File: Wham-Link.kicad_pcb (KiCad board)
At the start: 4 copper layers, 70 x 30 mm, 45 parts, among them J2 Conn_02x05_Counter_Clockwise, J3 Conn_01x09_Pin, SW2 SKRPACE010, SW3 SKRPACE010, U1 LAN8720A-CP-TR, U2 AMS1117-3.3, U3 CH340C, U4 ESP32-WROOM-32UE, X1 ECS-2520MV-250-CN-TR

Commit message: v0.1 Wham-Link for Layout Review
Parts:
- moved J2 0.30 mm to (175.8, 102.7)
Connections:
- J2 pad 1: GPI36 -> unconnected-(J2-Pin_1-Pad1)
- J2 pad 10: GP33 -> unconnected-(J2-Pin_10-Pad10)
- J2 pad 2: GPI39 -> unconnected-(J2-Pin_2-Pad2)
- J2 pad 3: GPI34 -> unconnected-(J2-Pin_3-Pad3)
- J2 pad 4: GPI35 -> unconnected-(J2-Pin_4-Pad4)
- J2 pad 6: GP14 -> unconnected-(J2-Pin_6-Pad6)
- J2 pad 7: GP16 -> GND
- J2 pad 8: GP17 -> unconnected-(J2-Pin_8-Pad8)
- J2 pad 9: GP32 -> unconnected-(J2-Pin_9-Pad9)
- J3 pad 2: unconnected-(J3-Pin_2-Pad2) -> +3V3
- J3 pad 3: unconnected-(J3-Pin_3-Pad3) -> GND
- J3 pad 4: unconnected-(J3-Pin_4-Pad4) -> GP14
- J3 pad 5: unconnected-(J3-Pin_5-Pad5) -> GP16
- J3 pad 6: unconnected-(J3-Pin_6-Pad6) -> GP13
- J3 pad 7: unconnected-(J3-Pin_7-Pad7) -> GP33
- J3 pad 8: unconnected-(J3-Pin_8-Pad8) -> GP32
- J3 pad 9: unconnected-(J3-Pin_9-Pad9) -> GP17
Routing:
- net +3V3: track 129.8 -> 3.32 mm, vias 4 -> 0
- net GND: track 2.55 -> 50.2 mm, vias 16 -> 36
- net Net-(U3-V3): track 15.2 -> 21.6 mm
- net GPI39: track 0.00 -> 1.71 mm, vias 0 -> 1
- net GPI36: track 0.00 -> 1.70 mm, vias 0 -> 1
- net GPI34: track 0.00 -> 1.70 mm, vias 0 -> 1
- net GP32: track 0.00 -> 1.61 mm, vias 0 -> 1
- net GP33: track 0.00 -> 1.60 mm, vias 0 -> 1
- net GPI35: track 0.00 -> 1.60 mm, vias 0 -> 1
- net IO23: track 46.4 -> 45.8 mm
- added copper zone on In1.Cu, net (none)
- added copper zone on F.Cu, net GND

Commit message: v0.1 Wham-Link for Layout Review + made some adjustments
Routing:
- net +5V: track 60.8 -> 0.00 mm, vias 2 -> 0

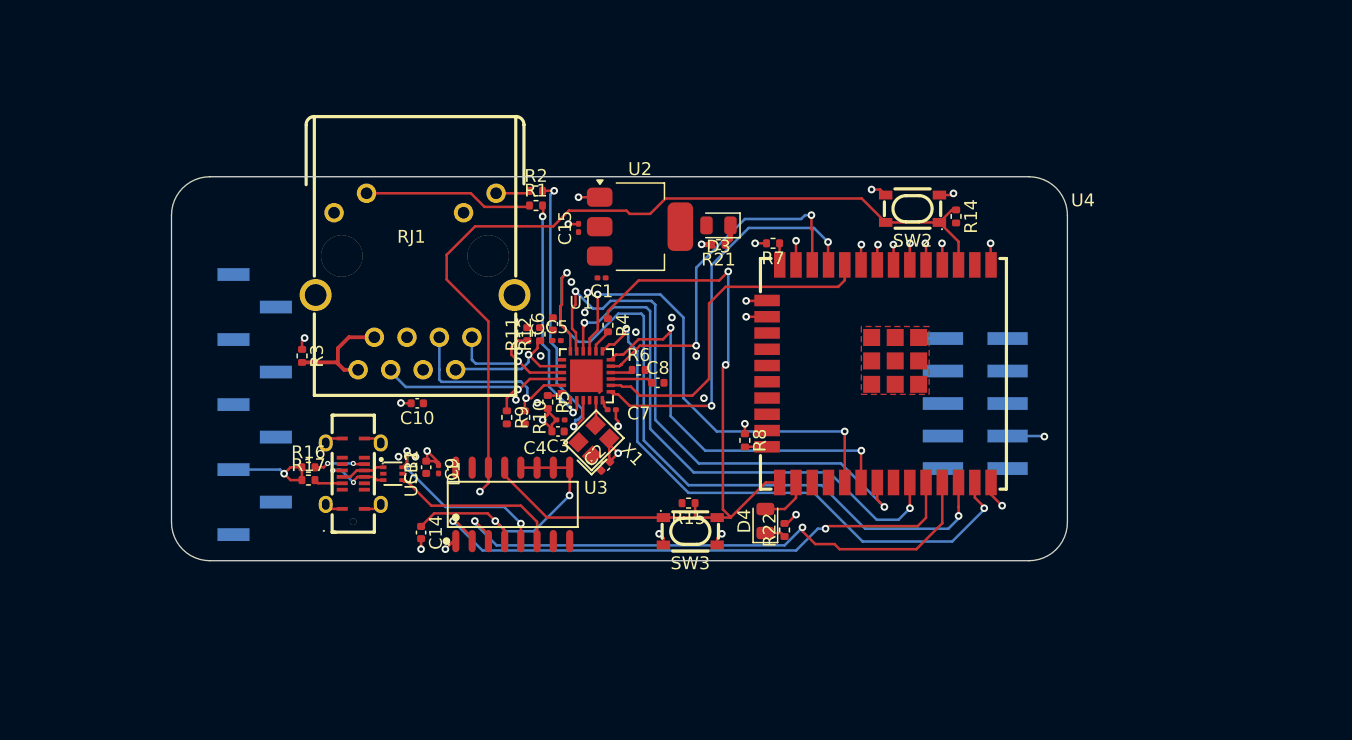
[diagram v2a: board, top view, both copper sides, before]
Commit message: Added unidirectional diodes to power supply and connected GPIOs to pinout
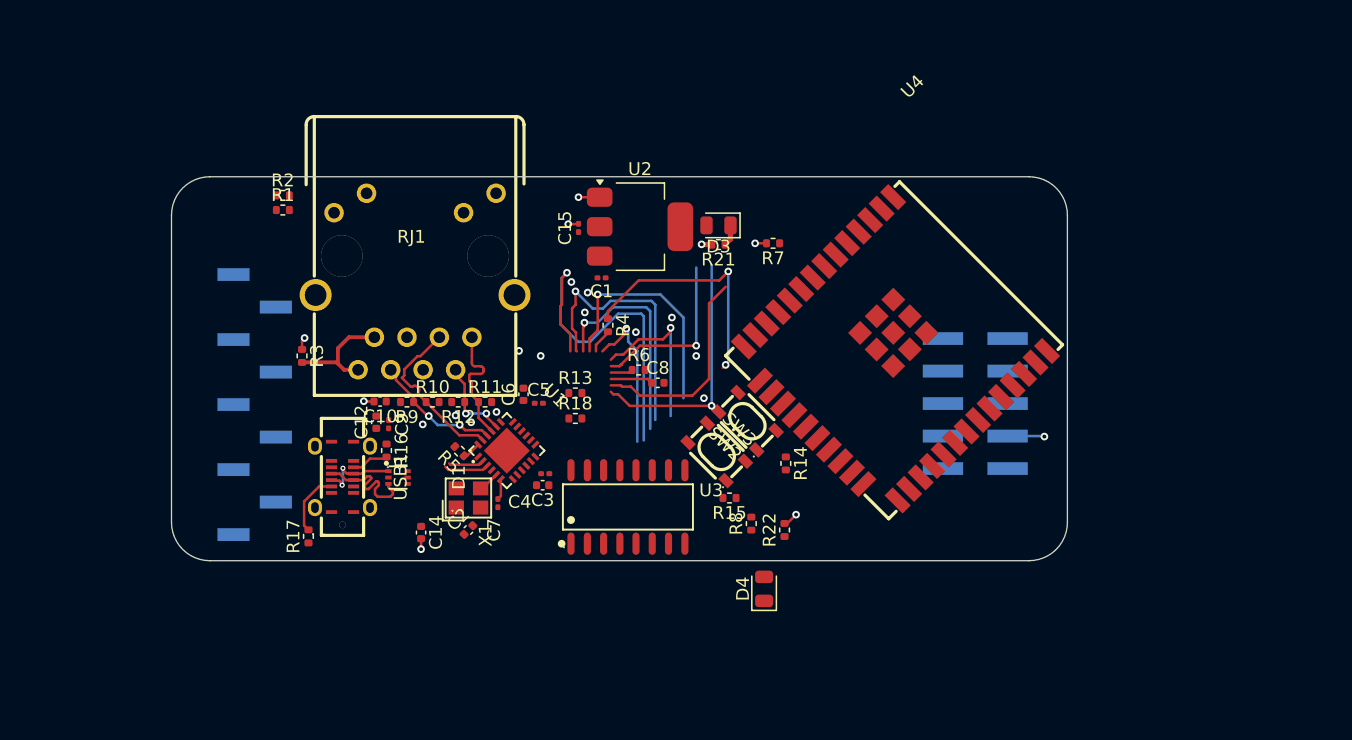
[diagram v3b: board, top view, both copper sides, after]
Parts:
- added R13: 0R, Resistor_SMD:R_0402_1005Metric, F.Cu at (144.6, 101.9)
- added R18: 0R, Resistor_SMD:R_0402_1005Metric, F.Cu at (144.6, 103.9)
- moved R14 23.4 mm to (161.0, 107.4)
- moved SW2 21.0 mm to (158.0, 104.1), turned to 135 degrees
- moved R1 19.8 mm to (121.7, 87.6)
- moved R2 19.8 mm to (121.7, 86.5)
- moved C2 11.8 mm to (136.2, 112.6)
- moved C7 11.5 mm to (138.5, 110.5), turned to -90 degrees
- moved X1 10.8 mm to (136.2, 110.1), turned to 0 degrees
- moved U3 9.00 mm to (148.7, 110.8)
- moved U1 8.54 mm to (139.2, 106.4), turned to -45 degrees
- moved R12 8.31 mm to (135.4, 102.6), turned to 180 degrees
- moved R5 7.90 mm to (135.5, 106.4), turned to 135 degrees
- moved R9 7.89 mm to (131.4, 102.6), turned to 180 degrees
- moved R10 7.30 mm to (133.4, 102.6), turned to 0 degrees
- moved SW3 6.53 mm to (155.6, 106.5), turned to 135 degrees
- moved R8 6.52 mm to (158.3, 112.1), turned to 90 degrees
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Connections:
- C10 pad 1: +3V3 -> Net-(C10-Pad1)
- RJ1 pad 4: +3V3 -> Net-(R13-Pad1)
- RJ1 pad 5: +3V3 -> Net-(R13-Pad1)
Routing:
- net RESET: track 67.1 -> 19.3 mm
- net TXD0: track 44.9 -> 0.00 mm, vias 2 -> 0
- net RXD0: track 44.0 -> 0.00 mm, vias 2 -> 0
- net GND: track 50.2 -> 11.8 mm, vias 36 -> 22
- net BOOT: track 56.6 -> 19.0 mm
- net IO23: track 45.8 -> 12.0 mm, vias 2 -> 1
- net IO26: track 31.9 -> 0.00 mm, vias 2 -> 0
- net IO22: track 59.3 -> 28.6 mm, vias 2 -> 1
- net IO21: track 42.9 -> 17.2 mm, vias 2 -> 1
- net IO19: track 44.0 -> 21.1 mm, vias 2 -> 1
- net Net-(U3-V3): track 21.6 -> 0.00 mm, vias 2 -> 0
- net LED1: track 23.3 -> 3.50 mm, vias 2 -> 0
- net IO18: track 31.3 -> 12.8 mm, vias 2 -> 1
- net IO5: track 36.1 -> 18.4 mm, vias 2 -> 1
- net LED2: track 18.3 -> 2.78 mm, vias 2 -> 0
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- removed copper zone on F.Cu, net GND

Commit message: Added footprints and 3D models for diodes, test points, and ferrite
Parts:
- added D2: D_Small_Filled, Diode_SMD:D_0402_1005Metric, F.Cu at (159.2, 75.4)
- added D6: D_Small_Filled, Diode_SMD:D_0402_1005Metric, F.Cu at (159.2, 77.4)
- added D7: D_Small_Filled, Diode_SMD:D_0402_1005Metric, F.Cu at (159.2, 79.4)
- added D8: D_Small_Filled, Diode_SMD:D_0402_1005Metric, F.Cu at (159.2, 81.4)
- added FB1: FerriteBead_Small, Ferrite_THT:LairdTech_28C0236-0JW-10, F.Cu at (150.5, 78.9)
- moved C14 9.44 mm to (141.9, 113.7)
- moved R7 8.91 mm to (155.7, 98.0), turned to 135 degrees
- moved R8 6.11 mm to (164.4, 111.7)
- moved D4 4.23 mm to (159.8, 113.0)
- moved C4 1.84 mm to (141.3, 109.8), turned to -90 degrees
- moved R22 1.21 mm to (161.4, 113.7)
- moved C5 1.00 mm to (141.8, 101.7)
- moved C3 0.92 mm to (142.2, 110.0), turned to -90 degrees
- moved C6 0.80 mm to (140.5, 101.2)
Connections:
- C12 pad 1: +5V -> Net-(D6-A)
- C9 pad 2: +5V -> Net-(D6-A)
- J2 pad 1: unconnected-(J2-Pin_1-Pad1) -> SCL
- J2 pad 2: unconnected-(J2-Pin_2-Pad2) -> GPI34
- J2 pad 3: unconnected-(J2-Pin_3-Pad3) -> SDA
- J2 pad 4: unconnected-(J2-Pin_4-Pad4) -> GPI36
- J2 pad 5: +3V3 -> Net-(D7-A)
- J2 pad 6: unconnected-(J2-Pin_6-Pad6) -> GPI35
- J2 pad 9: unconnected-(J2-Pin_9-Pad9) -> GPI39
- J3 pad 1: unconnected-(J3-Pin_1-Pad1) -> Net-(D8-A)
- J3 pad 2: +3V3 -> Net-(D2-A)
- R8 pad 2: Net-(U4-IO2) -> SCL
- U2 pad 2: +3V3 -> Net-(U2-VO)
- U4 pad 24: Net-(U4-IO2) -> SCL
- U4 pad 26: GP4 -> SDA
- USB1 pad A4: +5V -> Net-(D6-A)
- USB1 pad A9: +5V -> Net-(D6-A)
- USB1 pad B4: +5V -> Net-(D6-A)
- USB1 pad B9: +5V -> Net-(D6-A)
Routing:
- net BOOT: track 19.0 -> 0.00 mm, vias 2 -> 0
- net IO25: track 16.3 -> 0.93 mm, vias 0 -> 1
- net GND: track 11.8 -> 8.88 mm, vias 22 -> 17
- net IO21: track 17.2 -> 19.3 mm, vias 1 -> 2
- net Net-(U1-nINT/REFCLKO): track 1.92 -> 3.61 mm, vias 0 -> 1
- net IO27: track 13.5 -> 15.2 mm, vias 1 -> 2
- net IO18: track 12.8 -> 14.4 mm, vias 1 -> 2
- net IO5: track 18.4 -> 20.0 mm, vias 1 -> 2
- net IO19: track 21.1 -> 22.6 mm, vias 1 -> 2
- net IO23: track 12.0 -> 13.2 mm, vias 1 -> 2
- net Net-(U1-RXER/PHYAD0): track 1.75 -> 2.78 mm, vias 0 -> 1
- net IO22: track 28.6 -> 29.6 mm, vias 1 -> 2
- net IO26: track 0.00 -> 0.89 mm, vias 0 -> 1

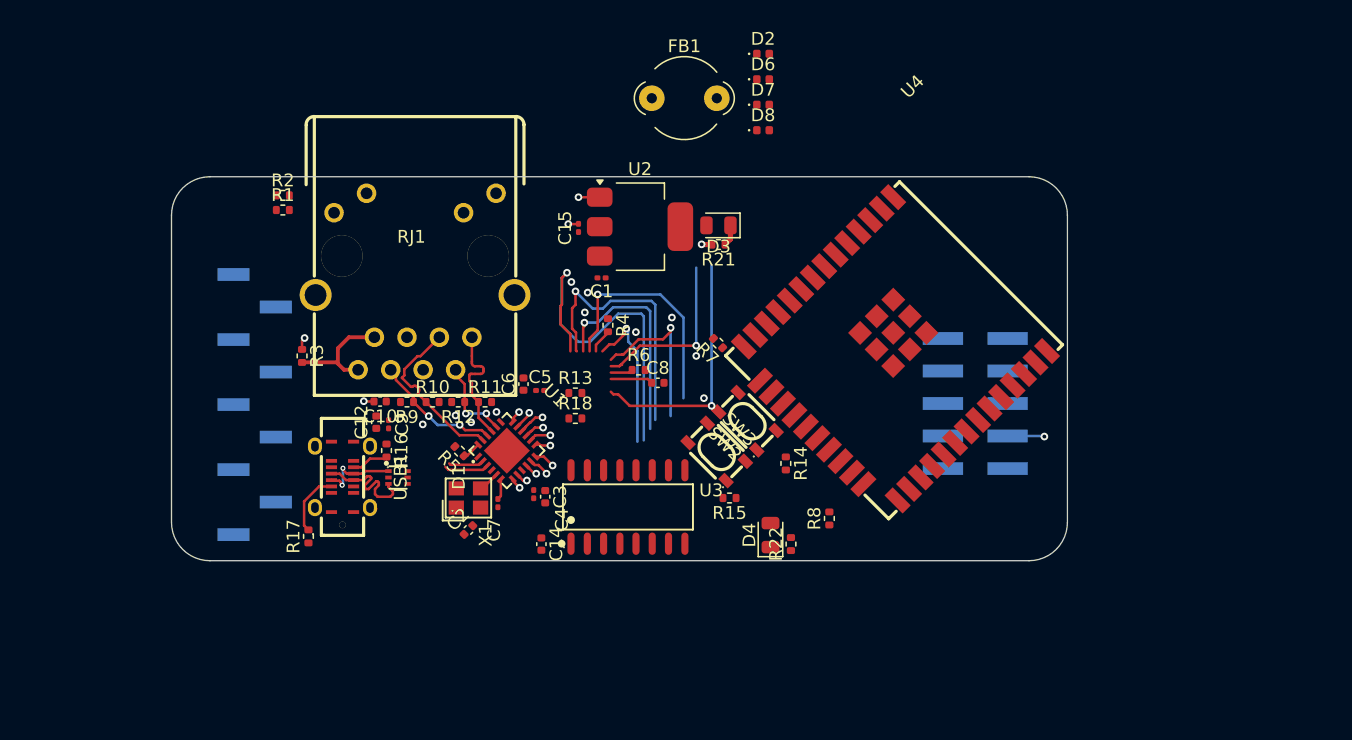
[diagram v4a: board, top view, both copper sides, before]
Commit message: Working on two-NPN transistor auto-reset circuit
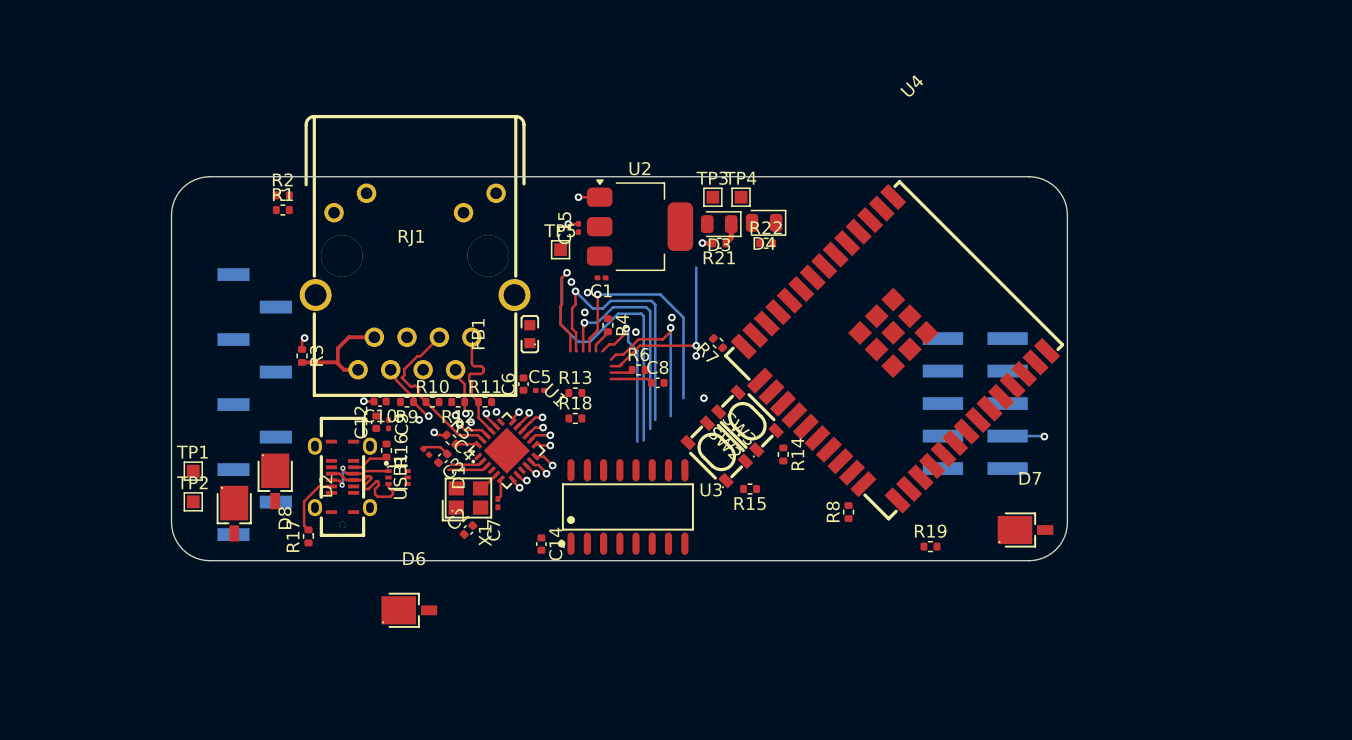
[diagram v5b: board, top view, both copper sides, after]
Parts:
- added R19: 10k, Resistor_SMD:R_0402_1005Metric, F.Cu at (172.3, 113.9)
- added TP1: TestPoint_Small, TestPoint:TestPoint_Pad_1.0x1.0mm, F.Cu at (114.7, 108.0)
- added TP2: TestPoint_Small, TestPoint:TestPoint_Pad_1.0x1.0mm, F.Cu at (114.7, 110.4)
- added TP3: TestPoint_Small, TestPoint:TestPoint_Pad_1.0x1.0mm, F.Cu at (155.3, 86.6)
- added TP4: TestPoint_Small, TestPoint:TestPoint_Pad_1.0x1.0mm, F.Cu at (157.5, 86.6)
- added TP5: TestPoint_Small, TestPoint:TestPoint_Pad_1.0x1.0mm, F.Cu at (143.4, 90.7)
- D2, D6, D7, D8: footprint Diode_SMD:D_0402_1005Metric -> imported-project-library:DIO-SMD_L2.0-W1.9-LS3.8-RD
- FB1: value FerriteBead_Small -> 120R@100MHz~0.05DCR; footprint Ferrite_THT:LairdTech_28C0236-0JW-10 -> imported-project-library:L0603
- moved D8 51.3 mm to (117.9, 111.7), turned to -90 degrees
- moved D2 50.9 mm to (121.1, 109.2), turned to -90 degrees
- moved D6 49.7 mm to (131.9, 118.9)
- moved D7 39.2 mm to (180.1, 112.6)
- moved D4 24.4 mm to (159.3, 88.6), turned to 180 degrees
- moved R22 23.6 mm to (159.5, 90.2), turned to 0 degrees
- moved FB1 20.8 mm to (141.0, 97.3), turned to 90 degrees
- moved C4 9.02 mm to (132.9, 106.5), turned to -45 degrees
- moved C3 8.54 mm to (134.2, 107.0), turned to -135 degrees
- moved R15 1.75 mm to (158.2, 109.4)
- moved R8 1.58 mm to (165.9, 111.2)
- moved R5 1.12 mm to (134.8, 105.5), turned to -45 degrees
- moved R14 0.73 mm to (160.8, 106.7)
- moved D3 0.12 mm to (155.8, 88.7)
- moved R21 0.12 mm to (155.8, 90.2)
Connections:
- C3 pad 1: +3V3 -> /VDD1A
- C4 pad 1: +3V3 -> /VDD1A
- C5 pad 1: +3V3 -> /VDD1A
- C6 pad 1: +3V3 -> /VDD1A
- D4 pad 2: GP4 -> GP14
- FB1 pad 1: +3V3 -> /VDD1A
- FB1 pad 2: Net-(U2-VO) -> +3V3
- R10 pad 2: +3V3 -> /VDD1A
- R11 pad 2: +3V3 -> /VDD1A
- R12 pad 2: +3V3 -> /VDD1A
- R5 pad 1: Net-(U1-RBIAS) -> GND
- R5 pad 2: GND -> Net-(U1-RBIAS)
- R9 pad 2: +3V3 -> /VDD1A
- U1 pad 1: +3V3 -> /VDD1A
- U1 pad 19: +3V3 -> /VDD1A
- U2 pad 2: Net-(U2-VO) -> +3V3
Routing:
- net RESET: track 19.3 -> 0.00 mm, vias 1 -> 0
- net /VDD1A: track 0.00 -> 2.14 mm
- net GND: track 8.88 -> 9.92 mm, vias 17 -> 18

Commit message: Added two-NPN transistor auto-reset to startup order and fixed UART bridge bug
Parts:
- added C16: 1uF, Capacitor_SMD:C_0402_1005Metric, F.Cu at (148.8, 122.2)
- added Q1: 2SC4617R, imported-project-library:SOT-523-3_L1.6-W0.8-P1.00-LS1.6-BR, F.Cu at (151.7, 122.3)
- added Q3: UMH3N, imported-project-library:SC-70-6_L2.2-W1.3-P0.65-LS2.1-BR, F.Cu at (152.1, 118.9)
- added R20: 10k, Resistor_SMD:R_0402_1005Metric, F.Cu at (148.9, 118.2)
- added R23: 4.7k, Resistor_SMD:R_0402_1005Metric, F.Cu at (148.9, 120.2)
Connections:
- net LED2 renamed /LED2
- R14 pad 1: RESET -> BOOT
- R15 pad 1: BOOT -> EN
- RJ1 pad 10: Net-(RJ1-LLED-) -> Net-(Q1-C)
- SW2 pad 1: RESET -> BOOT
- SW2 pad 2: RESET -> BOOT
- SW3 pad 1: BOOT -> EN
- SW3 pad 2: BOOT -> EN
- U1 pad 3: LED1 -> /LED1
- U3 pad 13: BOOT -> DTR
- U3 pad 14: RESET -> RTS
- U4 pad 3: RESET -> EN
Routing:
- net LED1: track 3.17 -> 0.00 mm
- net /LED1: track 0.00 -> 3.17 mm
